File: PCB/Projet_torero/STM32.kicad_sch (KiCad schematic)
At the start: 24 parts, among them J1 Conn_02x07_Odd_Even, J3 Conn_01x09, SW1 SW_Push, SW2 SW_Push, U1 STM32G431CBUx, Y1 Crystal_GND24_Small

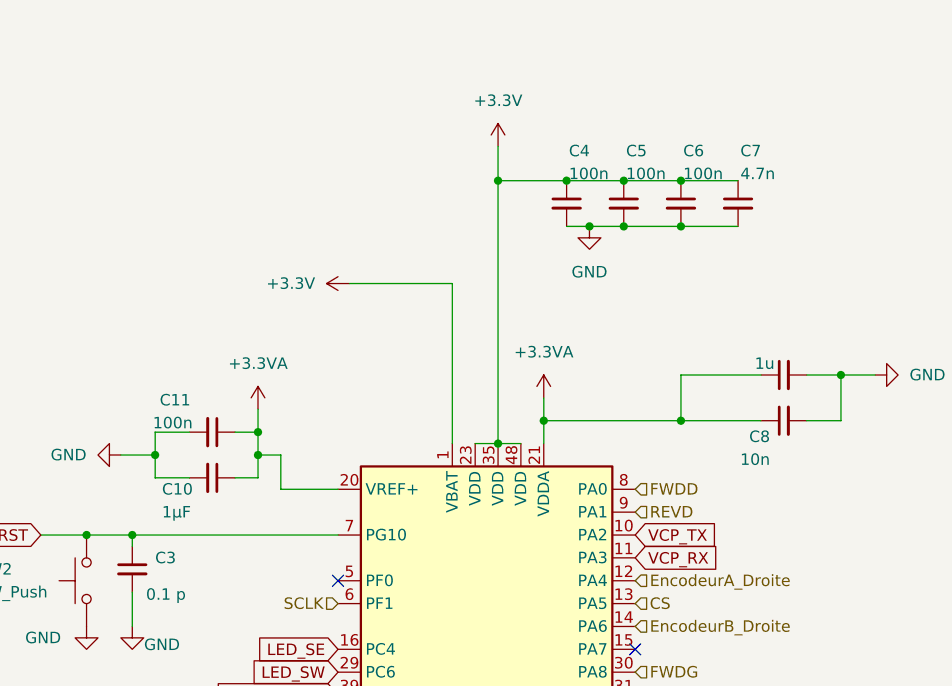
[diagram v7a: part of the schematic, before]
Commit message: modif valeur composants passifs
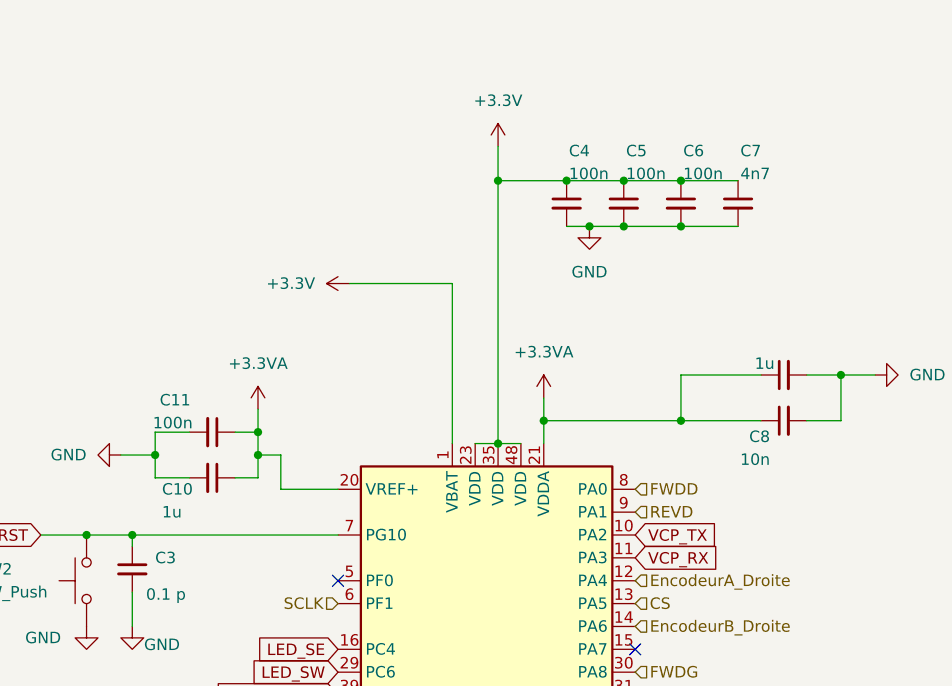
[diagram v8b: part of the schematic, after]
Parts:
- C10: value 1µF -> 1u
- C7: value 4.7n -> 4n7
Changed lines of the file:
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@@
 			)
 		)
-		(property "Value" "4.7n"
+		(property "Value" "4n7"
 			(at 122.174 36.068 0)
 			(effects
@@
 			)
 		)
-		(property "Value" "1µF"
+		(property "Value" "1u"
 			(at 57.912 73.66 90)
 			(effects
